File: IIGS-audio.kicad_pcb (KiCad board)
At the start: 2 copper layers, 65.8 x 46.6 mm, 39 parts, among them J1 Conn_01x07, J2 Conn_01x02_Male, J3 SJ1-3515N, J4 AppleII_slot, U1 74HC4052D, U2 TL074

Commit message: Added fiducial markers for pick and place machines.
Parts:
- added ?: , , F.Cu at (175.0, 115.3)
- added REF1: Fiducial_1mm_Mask2mm, Fiducial:Fiducial_1mm_Mask2mm, F.Cu at (114.9, 87.1)
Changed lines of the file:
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@@
     )
+  )
+  (footprint "" (layer "F.Cu")
+    (at 175.006 115.316)
+    (fp_text reference "" (at 0 0) (layer "F.SilkS")
+      (effects (font (size 1.27 1.27) (thickness 0.15)))
+    )
+    (fp_text value "" (at 0 0) (layer "F.SilkS")
+      (effects (font (size 1.27 1.27) (thickness 0.15)))
+    )
+    (pad "" smd circle (at 0 0) (size 1 1) (layers "F.Cu" "F.Mask")
+      (solder_mask_margin 0.5) (clearance 0.5))
   )
   (footprint "Resistor_SMD:R_0603_1608Metric" (layer "F.Cu")
@@
     )
   )
-  (footprint "Resistor_SMD:R_0603_1608Metric" (layer "F.Cu")
+  (footprint "Fiducial:Fiducial_1mm_Mask2mm" (layer "F.Cu")
+    (at 114.935 87.122)
+    (descr "Circular Fiducial, 1mm bare copper, 2mm soldermask opening (Level A)")
+    (tags "fiducial")
+    (attr smd board_only)
+    (fp_text reference "REF1" (at 0.254 -2.413) (layer "F.SilkS") hide
+      (effects (font (size 1 1) (thickness 0.15)))
+    )
+    (fp_text value "Fiducial_1mm_Mask2mm" (at 0 2) (layer "F.Fab")
+      (effects (font (size 1 1) (thickness 0.15)))
+    )
+    (fp_text user "${REFERENCE}" (at 0 0) (layer "F.Fab")
+      (effects (font (size 0.4 0.4) (thickness 0.06)))
+    )
+    (fp_circle (center 0 0) (end 1 0) (layer "F.Fab") (width 0.1) (fill none))
+    (pad "" smd circle (at 0 0) (size 1 1) (layers "F.Cu" "F.Mask")
+      (solder_mask_margin 0.5) (clearance 0.5))
+  )
+  (footprint "Resistor_SMD:R_0603_1608Metric" (layer "F.Cu")

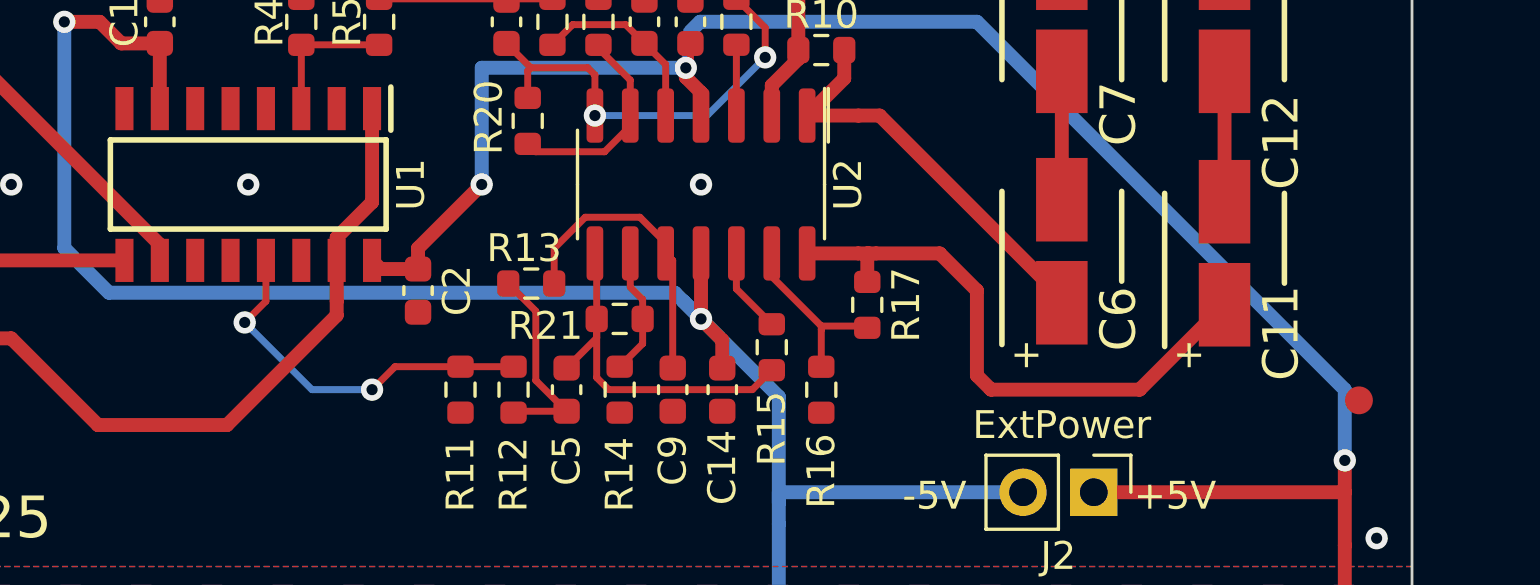
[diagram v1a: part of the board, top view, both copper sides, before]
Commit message: Adjusted fiducials for PnP machines.  Hid them under components.
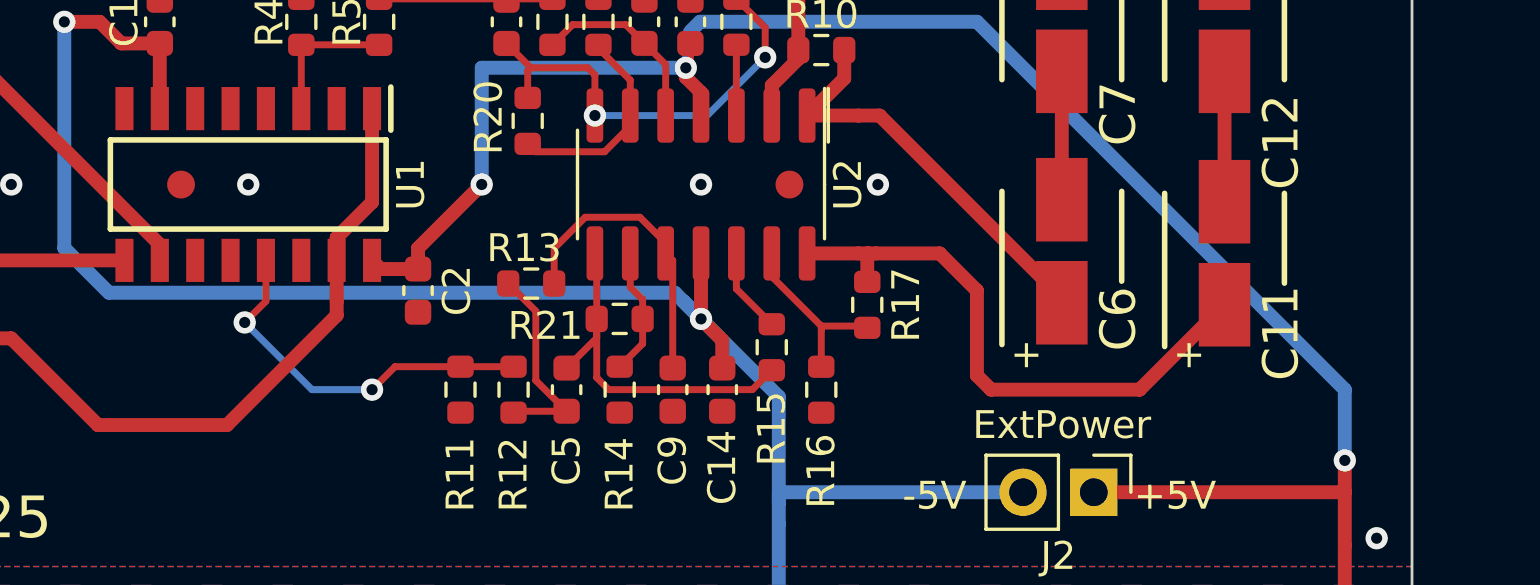
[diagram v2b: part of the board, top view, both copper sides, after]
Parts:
- added ?: , , F.Cu at (154.6, 107.6)
- moved ? 43.0 mm to (132.7, 107.6)
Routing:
- net GNDA: vias 7 -> 8
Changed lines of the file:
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@@
     )
+  )
+  (footprint "" (layer "F.Cu")
+    (at 154.559 107.569)
+    (fp_text reference "" (at 0 0) (layer "F.SilkS")
+      (effects (font (size 1.27 1.27) (thickness 0.15)))
+    )
+    (fp_text value "" (at 0 0) (layer "F.SilkS")
+      (effects (font (size 1.27 1.27) (thickness 0.15)))
+    )
+    (pad "" smd circle (at 0 0) (size 1 1) (layers "F.Cu" "F.Mask")
+      (solder_mask_margin 0.5) (clearance 0.5))
   )
   (footprint "Capacitor_SMD:C_0603_1608Metric" (layer "F.Cu")
@@
   )
   (footprint "" (layer "F.Cu")
-    (at 175.006 115.316)
+    (at 132.715 107.569)
     (fp_text reference "" (at 0 0) (layer "F.SilkS")
       (effects (font (size 1.27 1.27) (thickness 0.15)))
@@
   (via (at 126.619 107.5665) (size 0.8) (drill 0.4) (layers "F.Cu" "B.Cu") (free) (net 10))
   (via (at 112.395 84.824474) (size 0.8) (drill 0.4) (layers "F.Cu" "B.Cu") (free) (net 10))
+  (via (at 157.734 107.569) (size 0.8) (drill 0.4) (layers "F.Cu" "B.Cu") (free) (net 10))
   (via (at 112.395 120.2665) (size 0.8) (drill 0.4) (layers "F.Cu" "B.Cu") (free) (net 10))
   (via (at 175.641 84.824474) (size 0.8) (drill 0.4) (layers "F.Cu" "B.Cu") (free) (net 10))
